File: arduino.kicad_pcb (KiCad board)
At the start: 2 copper layers, 94 x 75.6 mm, 28 parts, among them IC1 ATMEGA32A-P, P1 PORT_D, P2 PORT_C, P3 PORT_B, P4 PORT_A, P5 ISP, P6 PWR, P7 BUS, P8 CONN_4, U1 74LS32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

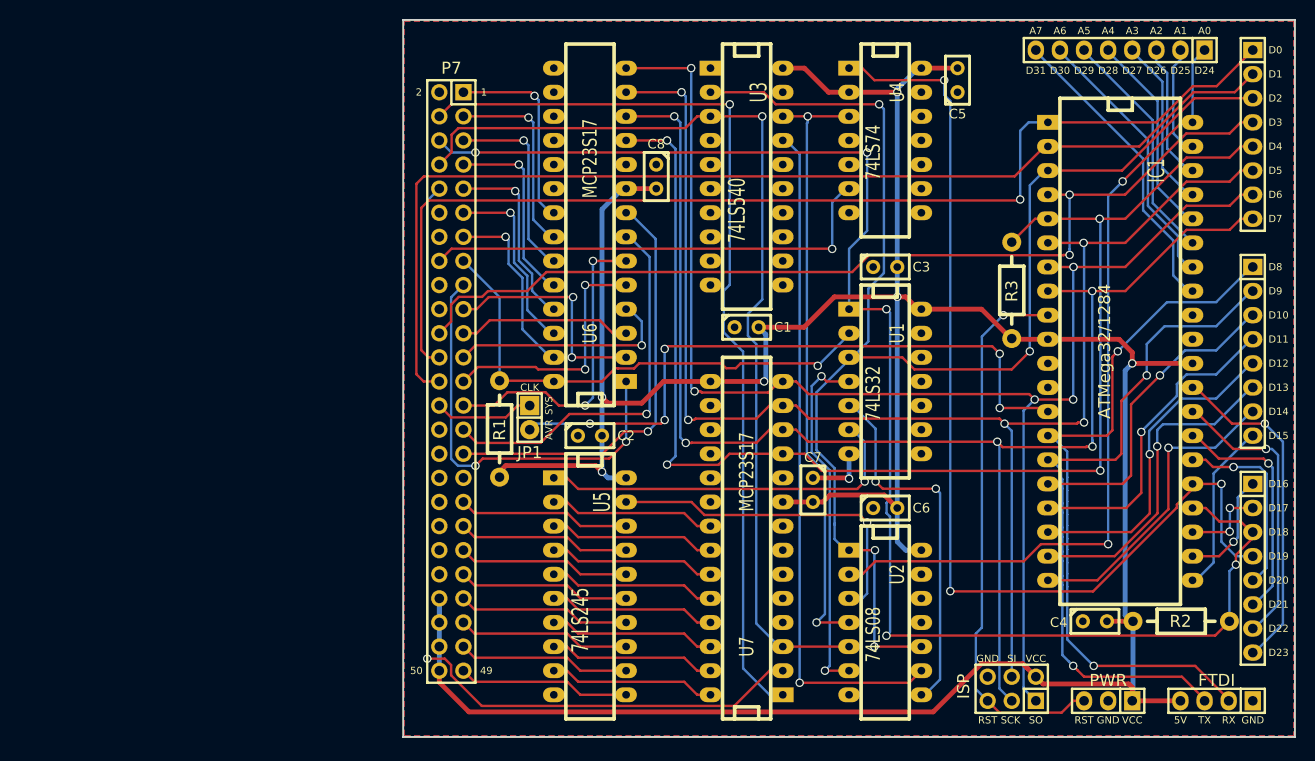
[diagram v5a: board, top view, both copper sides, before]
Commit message: Fix error with ISP port, and move data bus control from PortA to free that one up
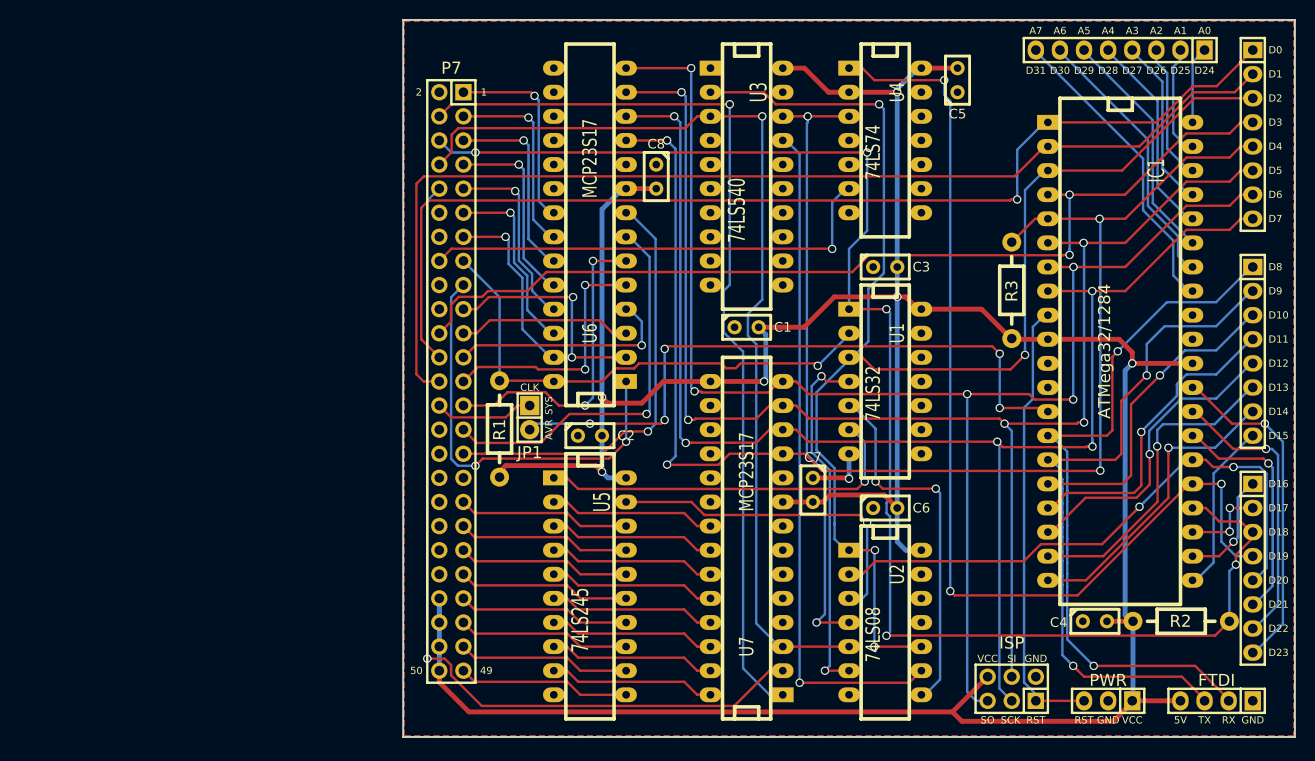
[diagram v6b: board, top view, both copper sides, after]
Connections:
- P5 pad 1: /DT6 -> /RST
- P5 pad 2: VCC -> GND
- P5 pad 5: /RST -> /DT6
- P5 pad 6: GND -> VCC
- U2 pad 2: /AN0 -> /DT20
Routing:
- net /AN0: track 85.6 -> 8.15 mm, vias 2 -> 0
- net /DT20: track 20.3 -> 61.5 mm, vias 1 -> 2
- net /RST: track 58.2 -> 47.5 mm, vias 1 -> 0
- net VCC: track 342.4 -> 344.5 mm
- net /BUSRQ: track 116.0 -> 114.1 mm
- net /DT12: track 34.1 -> 32.4 mm
- net /DT6: track 153.8 -> 155.0 mm
- net /DT13: track 34.1 -> 33.4 mm
- net /DT14: track 32.7 -> 32.0 mm

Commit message: Move some pins from AVR to one of the MCP:s to free up PORT A, C and D
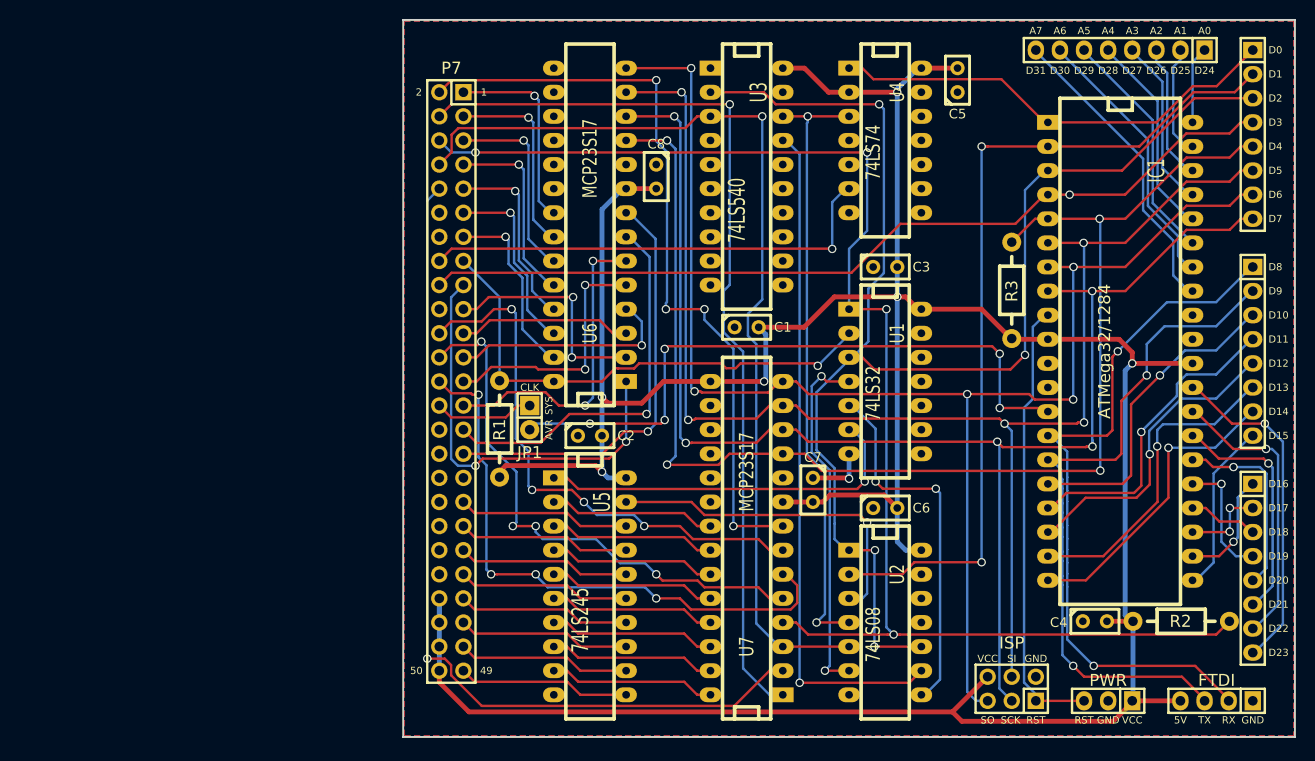
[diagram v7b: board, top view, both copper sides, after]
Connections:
- IC1 pad 1: /BUSRQ -> /CLRWT
- IC1 pad 2: /BUSAK -> /DENAB
- IC1 pad 25: /CLRWT -> /DT19
- P2 pad 4: /CLRWT -> /DT19
- P3 pad 1: /BUSRQ -> /CLRWT
- P3 pad 2: /BUSAK -> /DENAB
- P7 pad 18: /INT -> /DT3
- P7 pad 22: /DT3 -> /RESET
- P7 pad 6: /DT18 -> /IORQ
- R2 pad 2: /DT18 -> /IORQ
- U1 pad 1: /DT18 -> /IORQ
- U2 pad 2: /DT20 -> /DENAB
- U7 pad 4: Net-(U7-Pad4) -> /IORQ
- U7 pad 5: Net-(U7-Pad5) -> /BUSRQ
- U7 pad 6: Net-(U7-Pad6) -> /BUSAK
- U7 pad 7: Net-(U7-Pad7) -> /RESET
- U7 pad 8: Net-(U7-Pad8) -> /M1
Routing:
- net /IORQ: track 0.00 -> 149.6 mm, vias 0 -> 4
- net /DT18: track 156.5 -> 8.03 mm, vias 5 -> 0
- net /DENAB: track 0.00 -> 90.0 mm, vias 0 -> 2
- net /M1: track 0.00 -> 81.4 mm, vias 0 -> 4
- net /CLRWT: track 108.3 -> 48.1 mm, vias 3 -> 0
- net /RESET: track 0.00 -> 57.7 mm, vias 0 -> 4
- net /BUSRQ: track 114.1 -> 58.2 mm, vias 1 -> 4
- net /BUSAK: track 115.7 -> 62.2 mm, vias 0 -> 4
- net /DT20: track 61.5 -> 21.0 mm, vias 2 -> 1
- net /DT19: track 0.00 -> 13.4 mm, vias 0 -> 1
- net /DT3: track 102.0 -> 92.8 mm, vias 2 -> 1
